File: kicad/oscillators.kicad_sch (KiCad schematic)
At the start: 32 parts, among them U11 40106

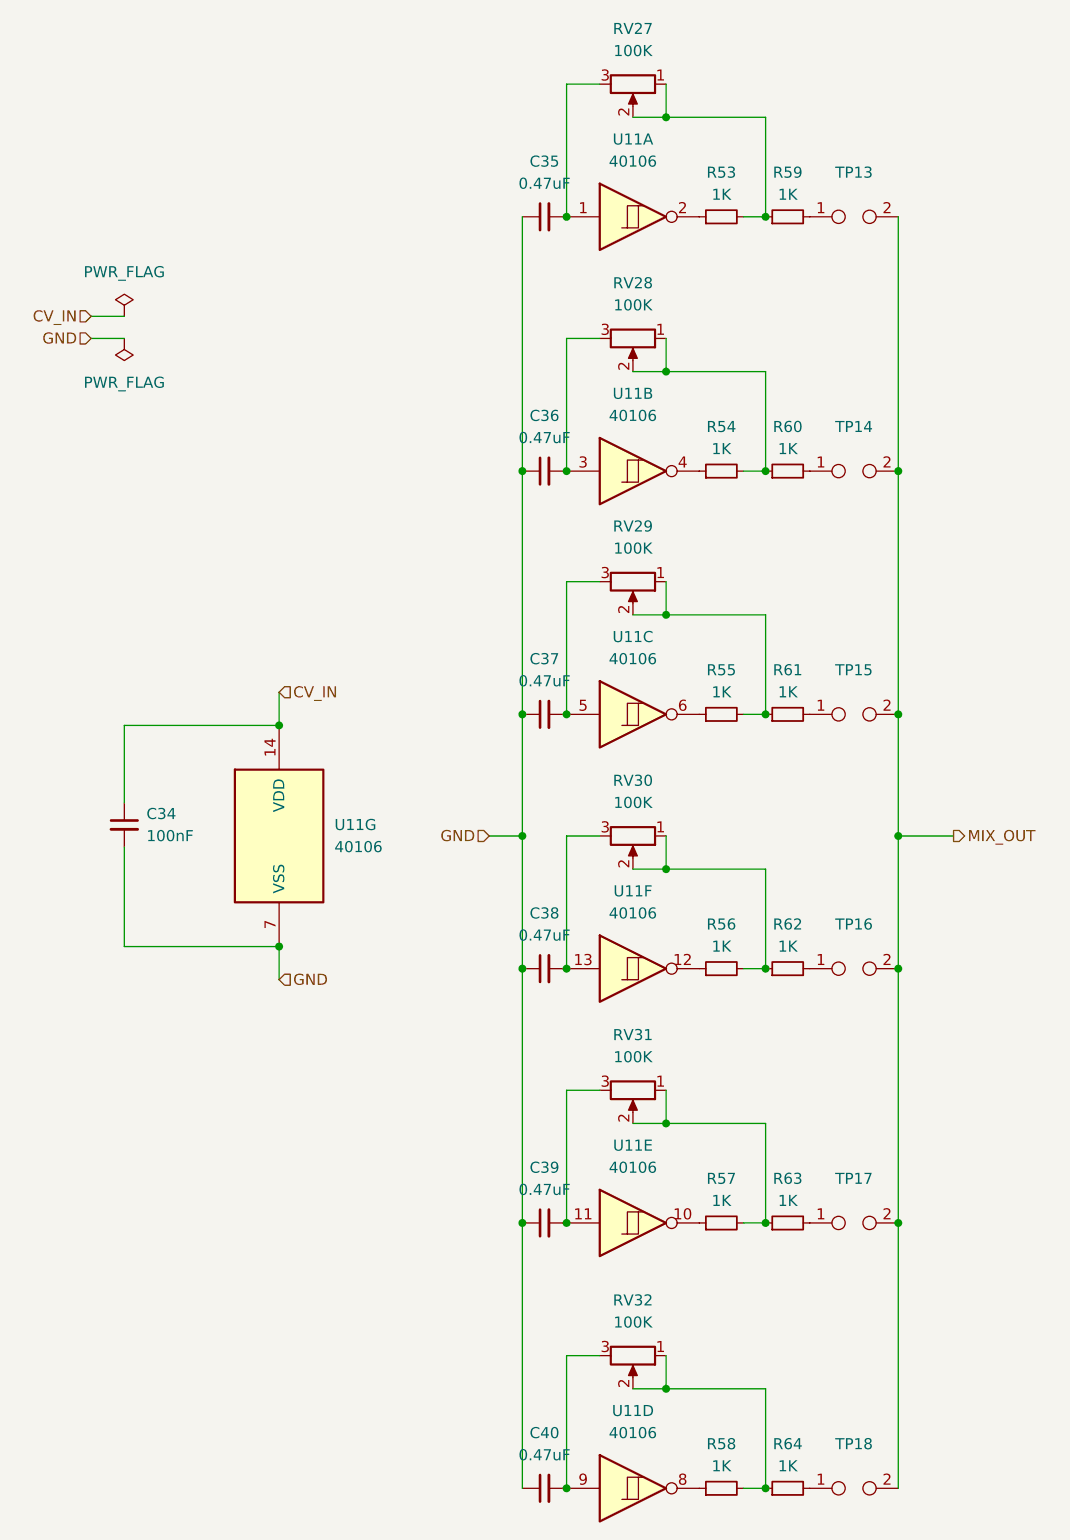
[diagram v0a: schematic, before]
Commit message: mark components as DNP, add LCSC part numbers
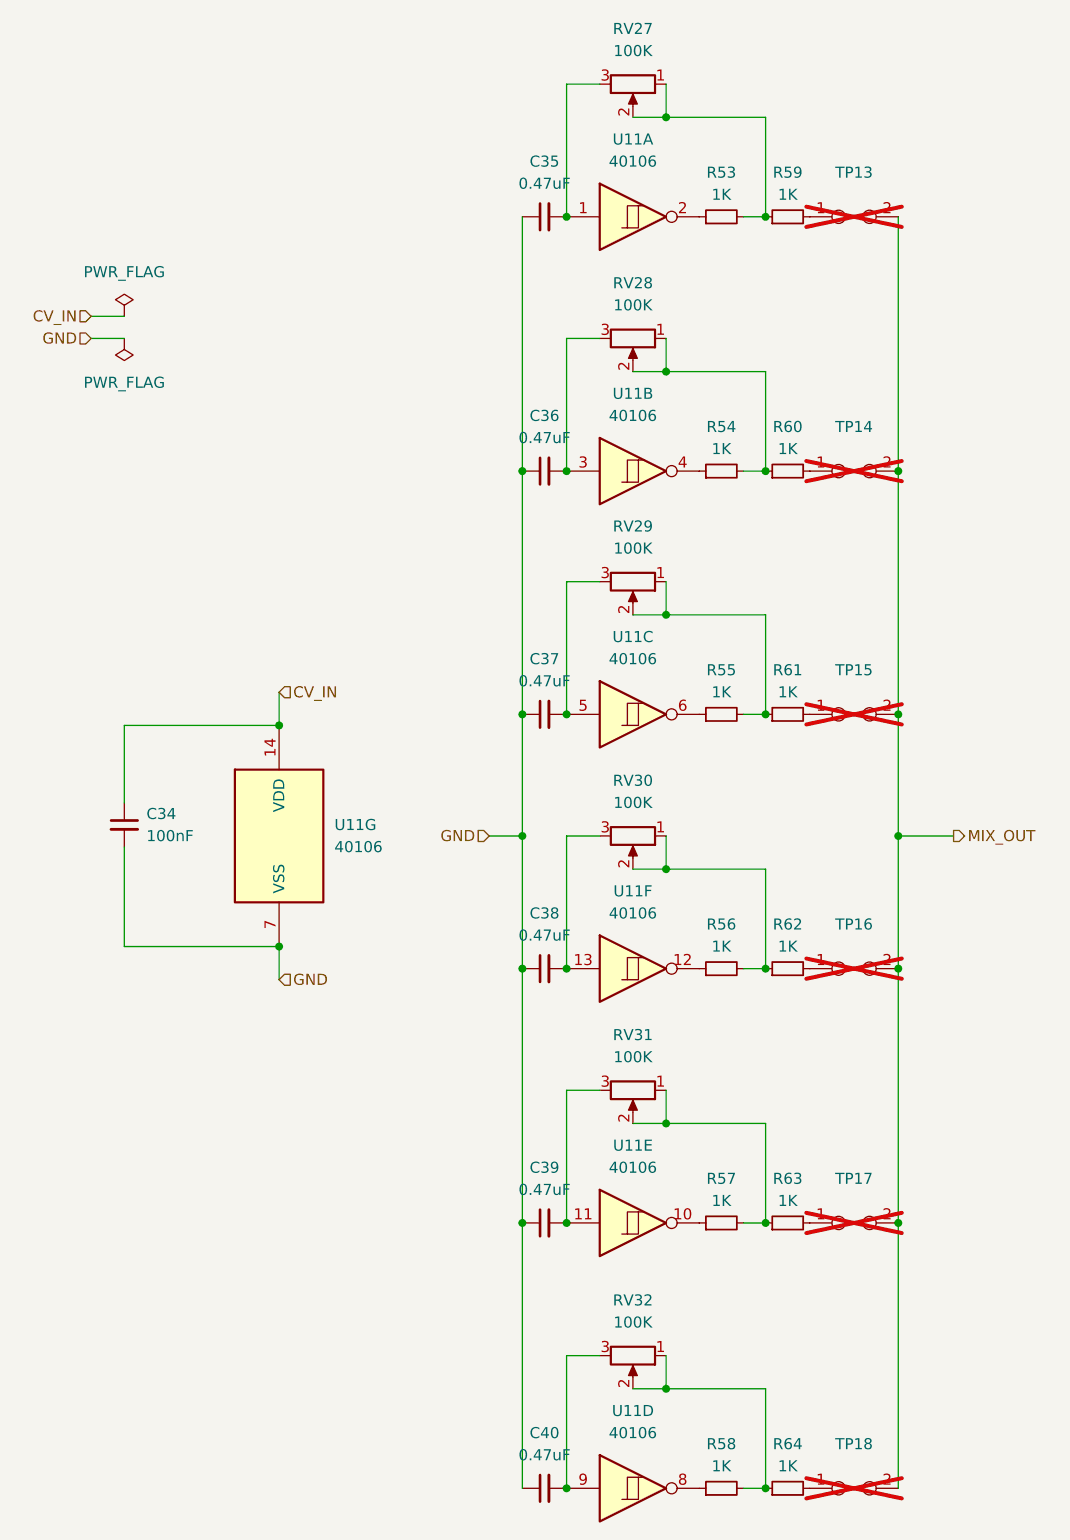
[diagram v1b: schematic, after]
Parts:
- TP13, TP14, TP15, TP16, TP17, TP18: now not fitted
- U11: JLC (none) -> C38184
